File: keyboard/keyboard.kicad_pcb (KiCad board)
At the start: 2 copper layers, 127.1 x 77.5 mm, 22 parts

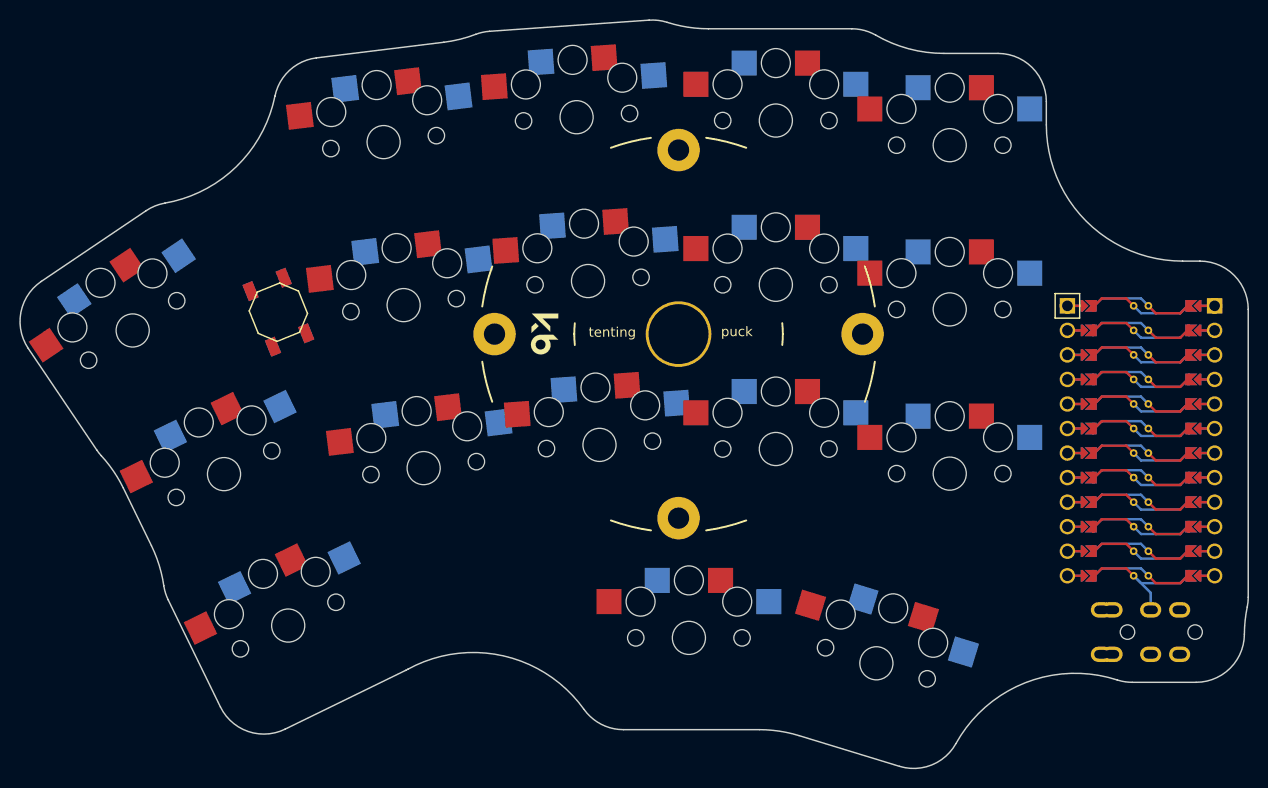
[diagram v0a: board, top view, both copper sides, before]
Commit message: Fix wrong connections
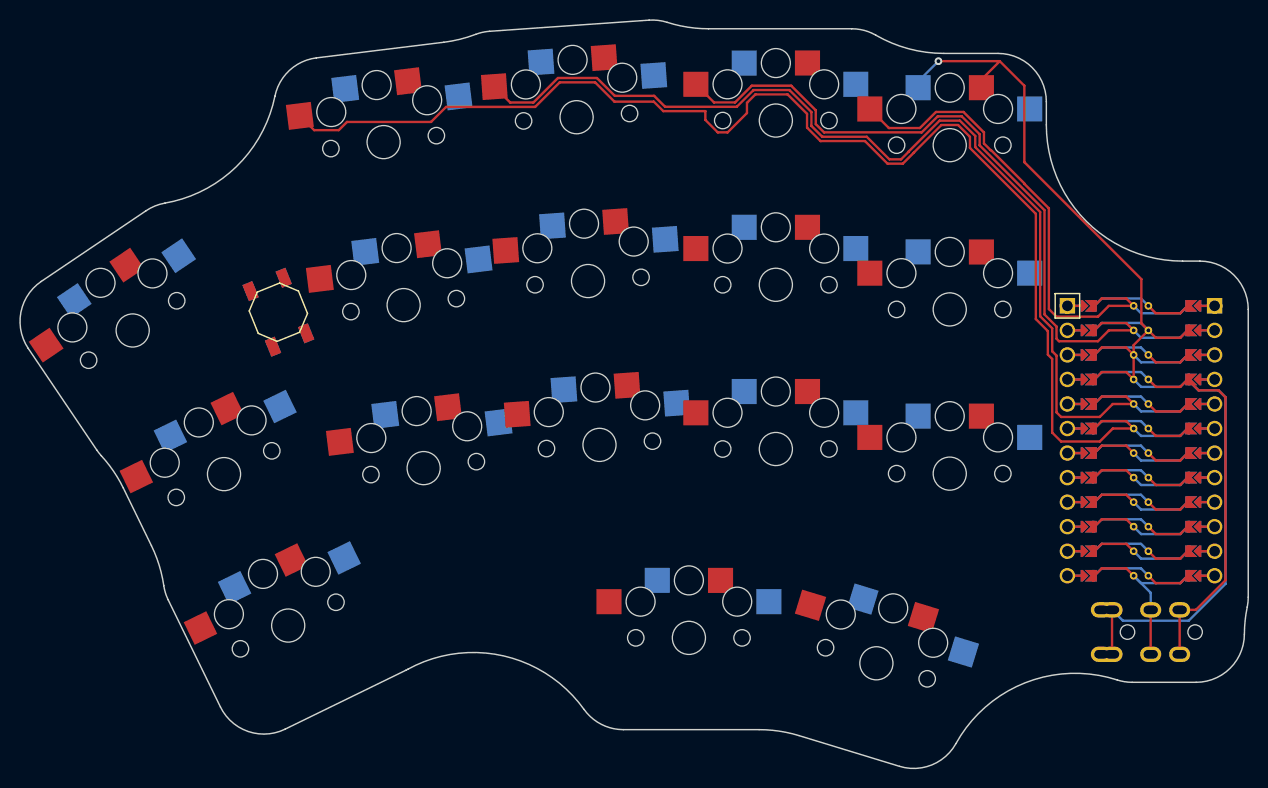
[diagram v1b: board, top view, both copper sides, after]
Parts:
- removed REF**: Tenting Puck, Library:TentingPuck
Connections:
- _1 pad 10: main_middle_bottom -> main_index_bottom
- _1 pad 11: main_index_bottom -> main_middle_bottom
- _1 pad 12: main_far_bottom -> main_ring_bottom
- _1 pad 19: main_far_home -> main_ring_top
- _1 pad 20: main_index_top -> main_middle_top
- _1 pad 23: main_middle_top -> main_index_top
- _1 pad 24: main_ring_top -> main_far_top
- _1 pad 5: main_ring_home -> main_far_home
- _1 pad 6: main_middle_home -> main_index_home
- _1 pad 7: main_index_home -> main_middle_home
- _1 pad 8: main_far_home -> main_ring_home
- _1 pad 9: main_ring_bottom -> main_far_bottom
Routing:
- net main_ring_top: track 0.00 -> 126.4 mm
- net main_middle_top: track 0.00 -> 100.4 mm
- net GND: track 0.00 -> 95.8 mm, vias 0 -> 1
- net main_index_top: track 0.00 -> 68.2 mm
- net main_far_top: track 0.00 -> 44.9 mm
- net VCC: track 0.00 -> 34.2 mm
- net P9: track 4.26 -> 8.86 mm

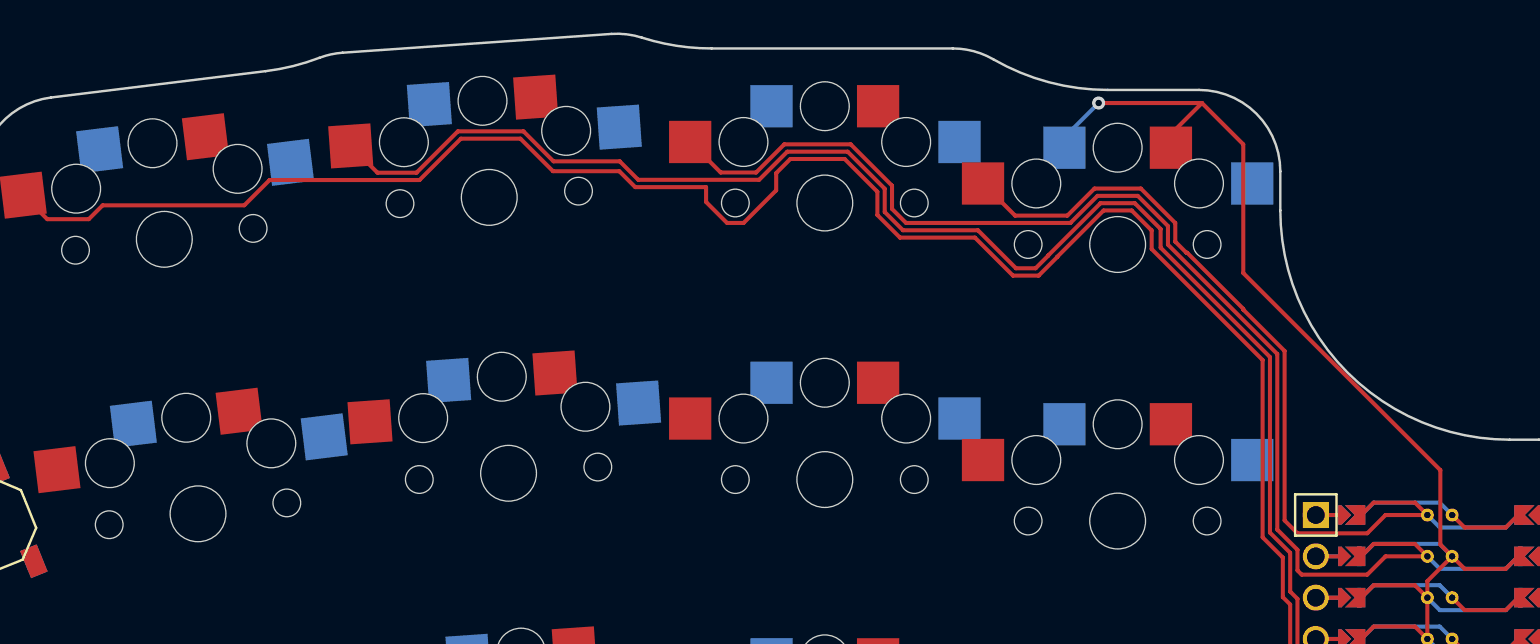
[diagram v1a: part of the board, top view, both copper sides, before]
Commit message: Route top row non-pinkie
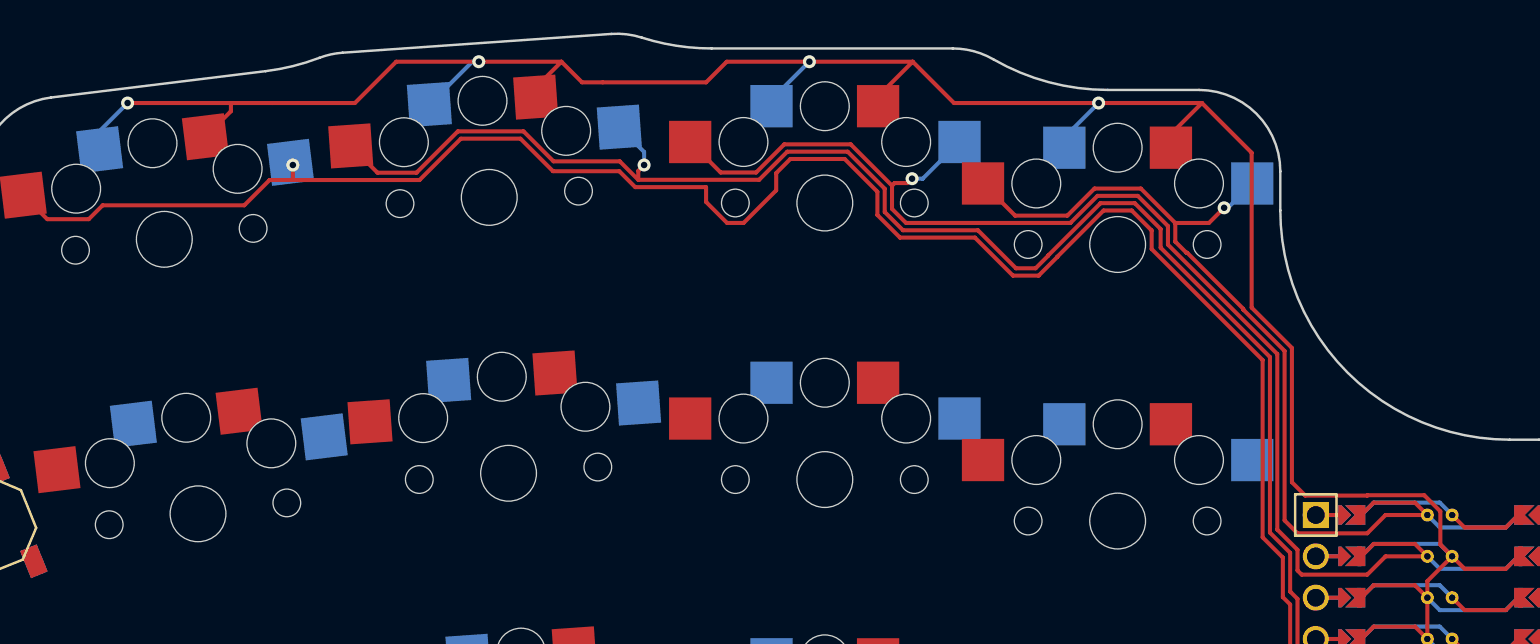
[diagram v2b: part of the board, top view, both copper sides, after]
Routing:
- net GND: track 95.8 -> 183.6 mm, vias 1 -> 4
- net main_far_top: track 44.9 -> 50.6 mm, vias 0 -> 1
- net main_index_top: track 68.2 -> 73.4 mm, vias 0 -> 1
- net main_middle_top: track 100.4 -> 104.5 mm, vias 0 -> 1
- net main_ring_top: track 126.4 -> 127.6 mm, vias 0 -> 1

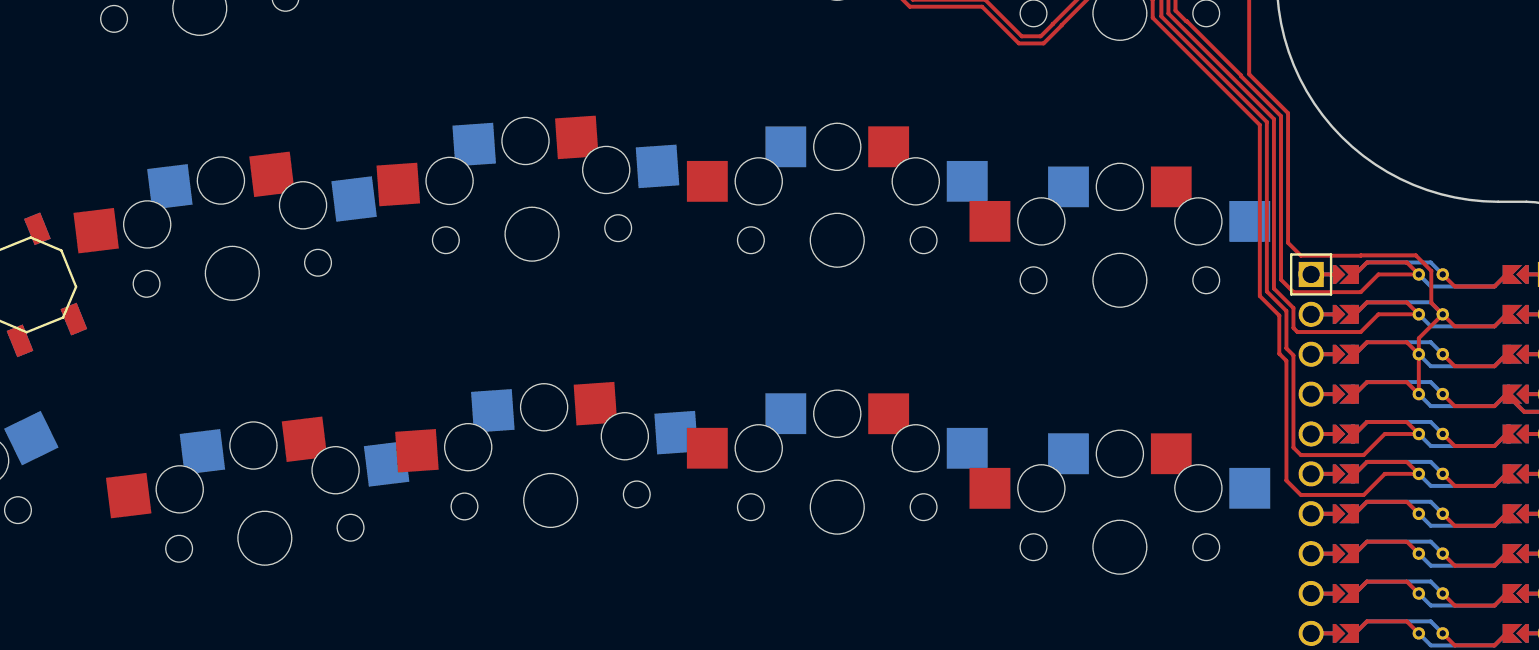
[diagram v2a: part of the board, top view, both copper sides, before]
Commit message: Route non-pinkie home row
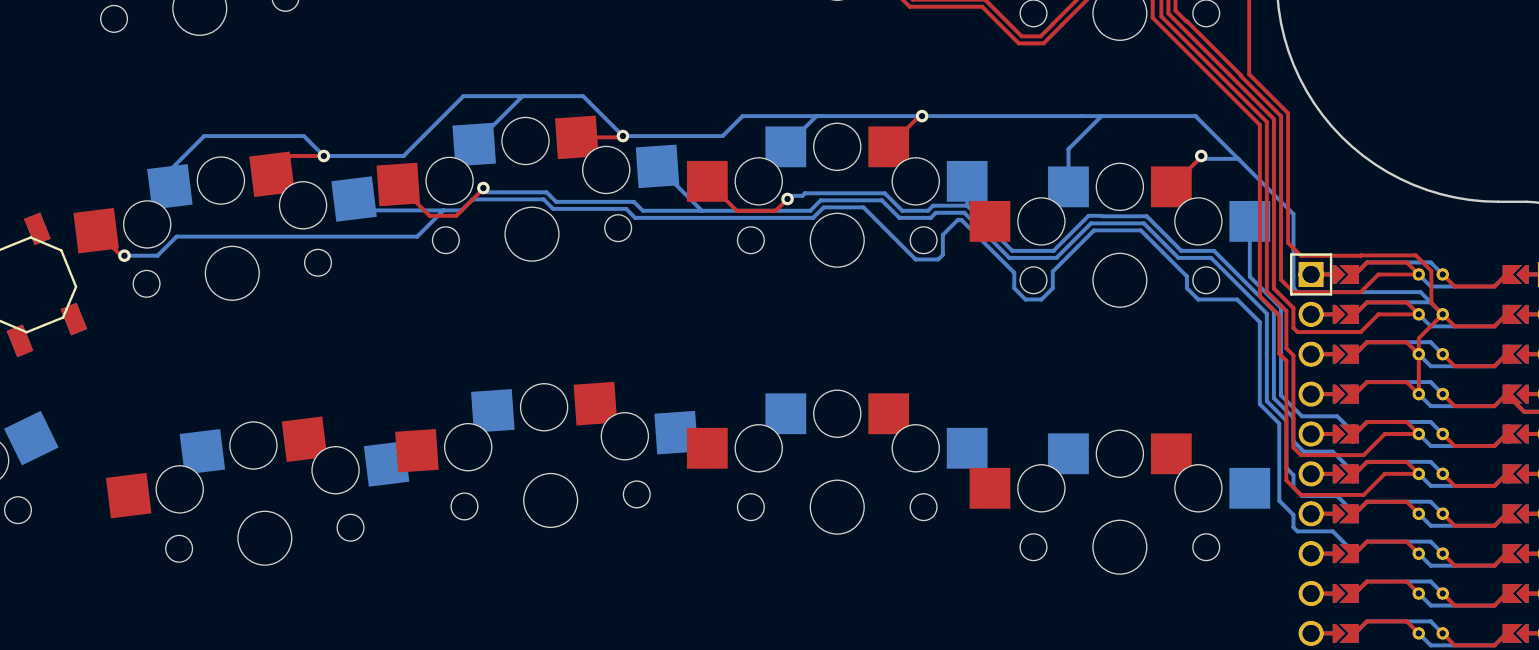
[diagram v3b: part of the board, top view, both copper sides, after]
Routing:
- net GND: track 183.6 -> 306.1 mm, vias 4 -> 8
- net main_ring_home: track 0.00 -> 112.7 mm, vias 0 -> 1
- net main_middle_home: track 0.00 -> 83.2 mm, vias 0 -> 1
- net main_index_home: track 0.00 -> 57.7 mm, vias 0 -> 1
- net main_far_home: track 0.00 -> 17.6 mm

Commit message: Clean up some stuff
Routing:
- net main_far_home: track 17.6 -> 38.6 mm, vias 0 -> 1
- net GND: track 306.1 -> 300.8 mm
- net main_ring_home: track 112.7 -> 110.5 mm
- net main_index_home: track 57.7 -> 56.4 mm
- net main_middle_home: track 83.2 -> 82.2 mm

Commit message: Connect the rest of the stuff
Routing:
- net GND: track 300.8 -> 623.8 mm, vias 8 -> 21
- net main_pinkie_top: track 0.00 -> 163.2 mm, vias 0 -> 1
- net main_pinkie_home: track 0.00 -> 139.3 mm, vias 0 -> 1
- net RST: track 0.00 -> 136.5 mm, vias 0 -> 1
- net main_pinkie_bottom: track 0.00 -> 111.8 mm, vias 0 -> 1
- net main_ring_bottom: track 0.00 -> 95.0 mm, vias 0 -> 1
- net main_middle_bottom: track 0.00 -> 74.0 mm, vias 0 -> 1
- net thumb_tucky: track 0.00 -> 63.5 mm, vias 0 -> 1
- net main_index_bottom: track 0.00 -> 52.2 mm, vias 0 -> 1
- net thumb_resty: track 0.00 -> 42.9 mm, vias 0 -> 1
- net main_far_bottom: track 0.00 -> 29.5 mm, vias 0 -> 1
- net main_ring_top: track 127.4 -> 123.1 mm
- net main_middle_top: track 104.5 -> 100.4 mm
- net main_index_top: track 73.4 -> 69.4 mm
- net main_far_top: track 50.6 -> 46.7 mm
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
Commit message: Fix some things
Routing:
- net GND: track 623.8 -> 617.6 mm
- net main_pinkie_top: track 163.2 -> 162.0 mm
- net main_middle_bottom: track 74.0 -> 73.2 mm
- net thumb_resty: track 42.9 -> 42.2 mm

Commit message: Tent puck and some cleanup
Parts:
- added REF**: Tenting Puck, Library:TentingPuck, F.Cu at (39.6, -31.4)
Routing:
- net GND: track 617.6 -> 627.6 mm
- net main_pinkie_top: track 162.0 -> 167.9 mm
- net main_pinkie_home: track 139.0 -> 144.9 mm
- net main_pinkie_bottom: track 111.4 -> 115.9 mm
